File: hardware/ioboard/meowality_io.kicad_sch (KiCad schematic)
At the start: 88 parts, among them J1 MINI_DP_SINK, J2 USB_C_Receptacle, J3 Conn_01x03, J4 Conn_01x05, J5 Conn_01x03, J6 JTAG, SW1 SW_SPDT, SW2 SW_Push, SW3 SW_Push, U1 TPD4E02B04DQA, U10 PCAL6416APW, U11 AP6230xWU, U12 LD3985M18R_SOT23, U13 HDSP-7501, U2 TPD4E02B04DQA, U3 FUSB302B11MPX, U4 CBTL02043A, U5 CH330N, U6 FE1.1s, U7 SiC438, U8 CH330N, U9 24LC00, Y1 12MHz

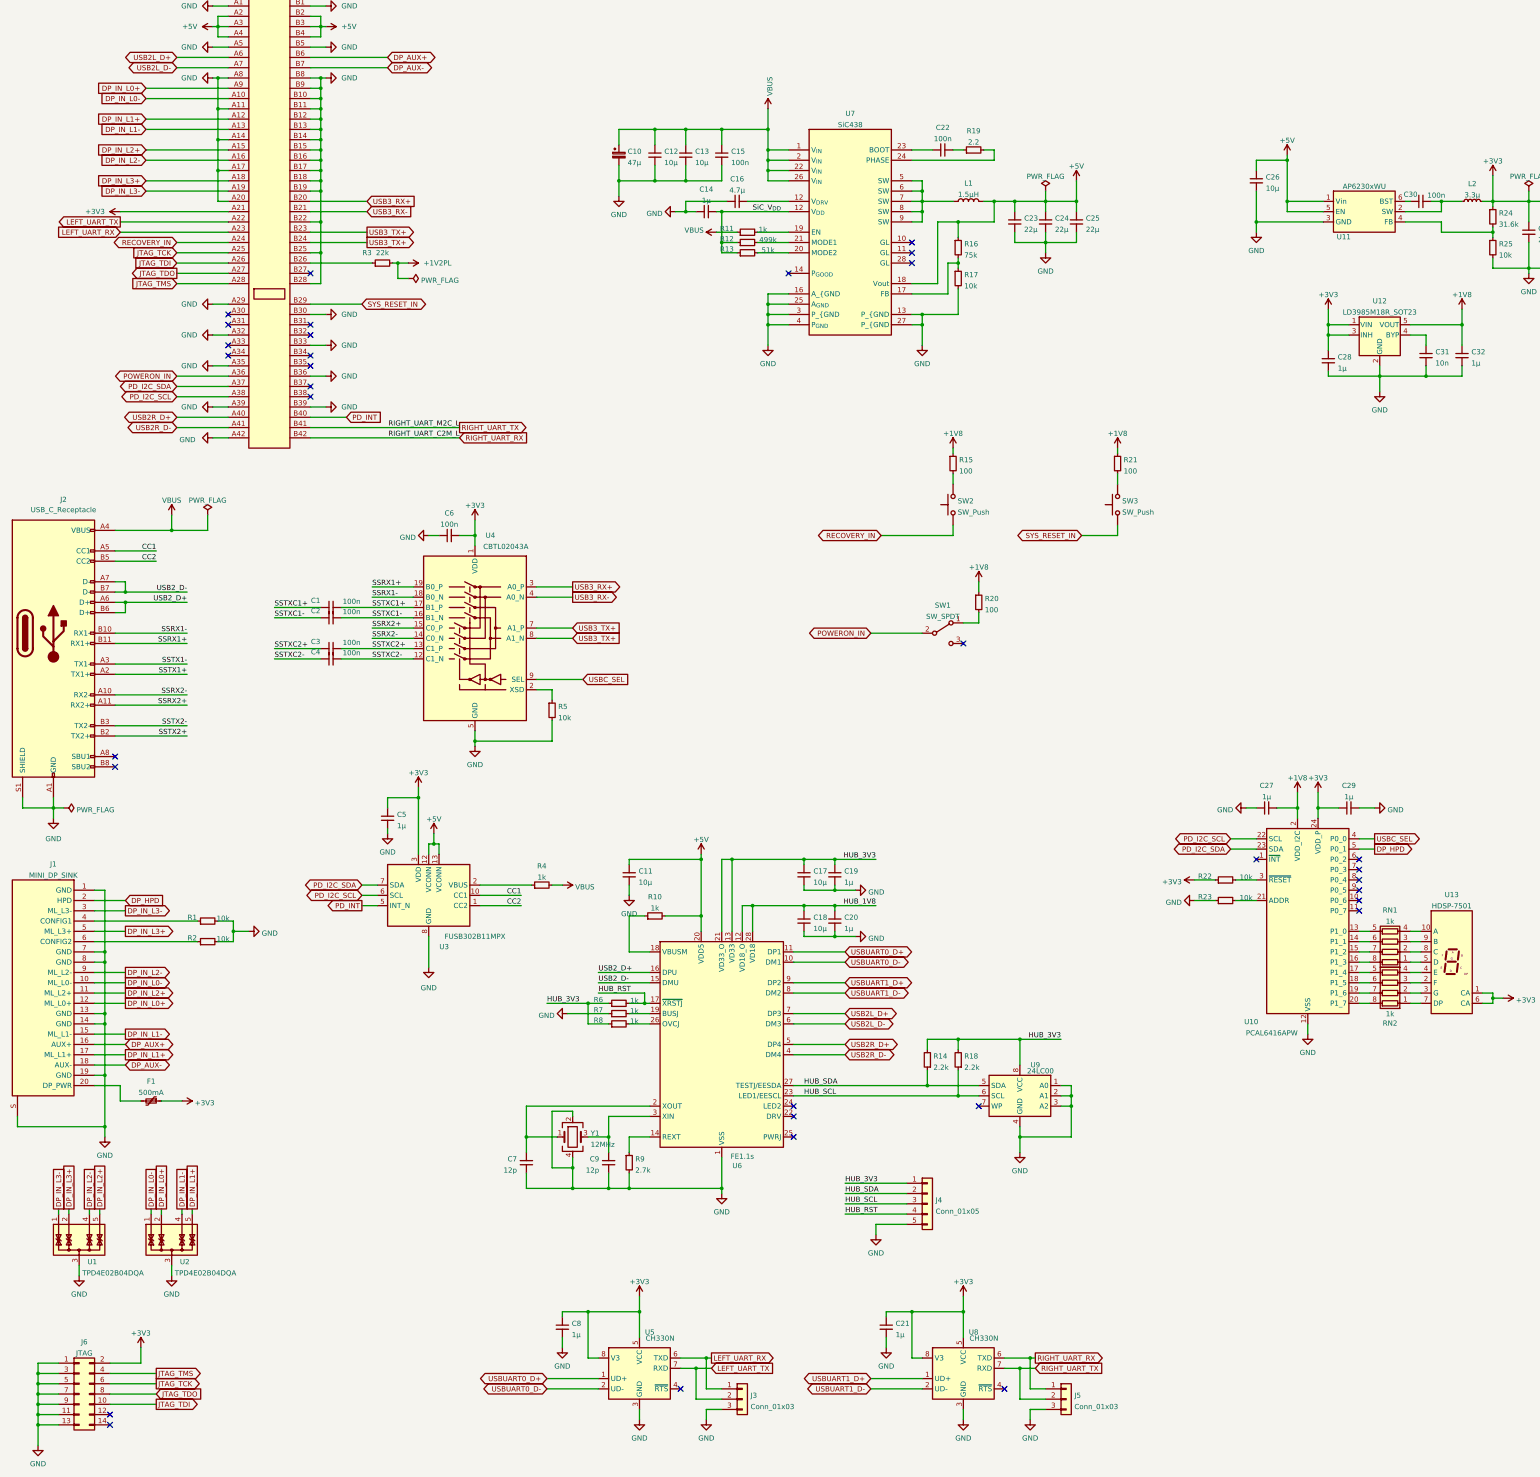
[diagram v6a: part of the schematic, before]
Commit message: Replace type-C power with good ol' barrel jack
Signed-off-by: gatecat <gatecat@ds0.me>
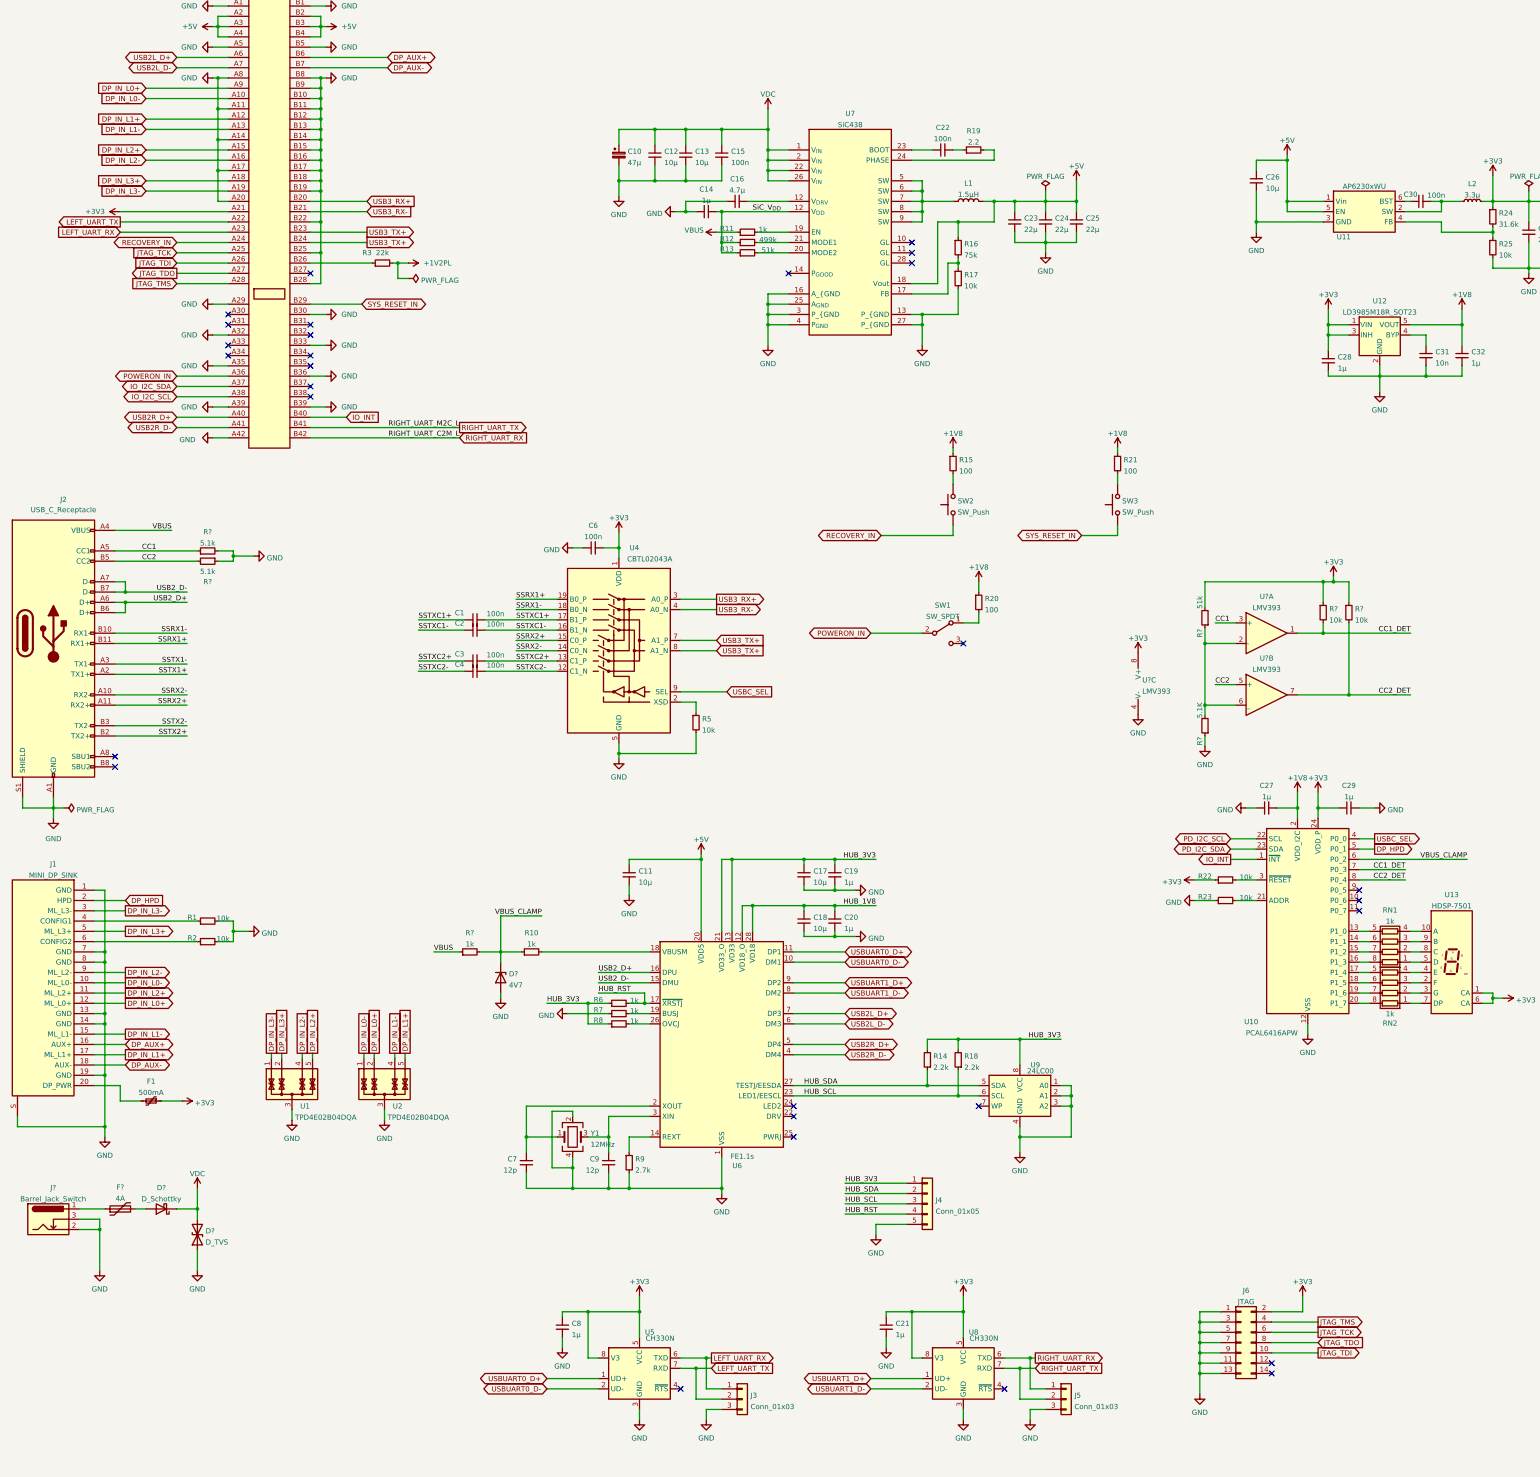
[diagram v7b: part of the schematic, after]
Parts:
- removed C5: 1µ, symbol Device:C_Small
- removed R4: 1k, symbol Device:R_Small
- removed U3: FUSB302B11MPX, Package_DFN_QFN:WQFN-14-1EP_2.5x2.5mm_P0.5mm_EP1.45x1.45mm, symbol Interface_USB:FUSB302B11MPX
- added D?: 4V7, symbol Device:D_Zener
- added D?: D_Schottky, symbol Device:D_Schottky
- added D?: D_TVS, symbol Device:D_TVS
- added F?: 4A, symbol Device:Polyfuse
- added J?: Barrel_Jack_Switch, symbol Connector:Barrel_Jack_Switch
- added R?: 51k, symbol Device:R_Small
- added R? (x2): 10k, symbol Device:R_Small
- added R?: 5.1K, symbol Device:R_Small
- added R?: 1k, symbol Device:R_Small
- added R? (x2): 5.1k, symbol Device:R_Small
- added U? (x3): LMV393, symbol Comparator:LMV393
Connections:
- net PD_INT is gone; now on net IO_INT: JL1.B40
- net +3V3: now also R?.1, R?.1, R?.2, U?.8 (V+)
- net +5V: no longer R10.2
- net CC1: now also R?.1, U?.3 (+)
- net CC2: now also R?.2, U?.5 (+)
- net GND: now also D?.1 (A1), D?.2 (A), J?.2, J?.3, R?.1, R?.1, R?.2, U?.4 (V-)
- net PD_I2C_SCL: no longer JL1.A38
- net PD_I2C_SDA: no longer JL1.A37
- net VBUS: now also R?.1; no longer C10.1, C12.1, C13.1, C15.1, U7.1 (V_{IN}), U7.2 (V_{IN}), U7.22 (V_{IN}), U7.26 (V_{IN})
- net at U6.18 (VBUSM): now also R10.2; no longer R10.1
- net IO_INT: now reaches U10.1 (~{INT})
- net VBUS_CLAMP: now reaches U10.6 (P0_2)
- net VBUS_CLAMP: now also R10.1, D?.1 (K), R?.2
- net CC1_DET: now reaches U10.7 (P0_3)
- net CC1_DET: now also R?.2, U?.1
- net CC2_DET: now reaches U10.8 (P0_4)
- net CC2_DET: now also R?.2, U?.7
- new net: R?.1, R?.2, U?.2 (-), U?.6 (_)
- new net: D?.2 (A), F?.2
- new net: F?.1, J?.1
- new net IO_I2C_SCL: JL1.A38
- new net IO_I2C_SDA: JL1.A37
- new net VDC: C10.1, C12.1, C13.1, C15.1, D?.1 (K), D?.2 (A2), U7.1 (V_{IN}), U7.2 (V_{IN}), U7.22 (V_{IN}), U7.26 (V_{IN})
- no-connect marks 33 -> 29
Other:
- moved on the sheet: C1, C2, C3, C4, C6, J6, R10, R5, U1, U2, U4
